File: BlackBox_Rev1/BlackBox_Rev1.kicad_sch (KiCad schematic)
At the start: 15 parts

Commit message: schematic design
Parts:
- removed C? (x2): 10uF, Capacitor_SMD:C_0603_1608Metric_Pad1.08x0.95mm_HandSolder, symbol Device:C
- removed SW?: SW_SP3T, MRDT_Connectors:MOLEX_uF_S_03_Vertical, symbol Switch:SW_SP3T
- removed U?: TSR1-2433, MRDT_Devices:TSR_1-2433, symbol Driveboard_2022-rescue:TSR1-2433-MRDT_Devices
- added C?: 1uF, Capacitor_SMD:C_0603_1608Metric_Pad1.08x0.95mm_HandSolder, symbol Device:C
- added C?: 22uF, Capacitor_THT:CP_Radial_D5.0mm_P2.00mm, symbol BMS_2022_Rev1-rescue:CP1-Device
- added C?: 10uF, Capacitor_SMD:C_0603_1608Metric_Pad1.08x0.95mm_HandSolder, symbol Device:C
- added D?: D, symbol Device:D
- added J?: Conn_02x08_Counter_Clockwise, symbol Connector_Generic:Conn_02x08_Counter_Clockwise
- added J?: Conn_02x05_Counter_Clockwise, symbol Connector_Generic:Conn_02x05_Counter_Clockwise
- added Q?: Q_PMOS_DGS, symbol Device:Q_PMOS_DGS
- added U?: TSR1-2433, MRDT_Devices:TSR_1-2433, symbol BMS_2022_Rev1-rescue:TSR1-2433-MRDT_Devices
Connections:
- net +12V: now also C?.1, U?.1 (Vin)
- net +3V3: now also C?.1, C?.1, D?.1 (K), D?.2 (A), J?.10 (Pin_10), J?.3 (Pin_3), Q?.1 (D), Q?.2 (G), Q?.3 (S), U?.3 (Vout)
- net GND: now also C?.2, C?.2, C?.2, J?.4 (Pin_4), J?.5 (Pin_5), U?.2 (GND)
- net Display_A: now reaches U?.0 (RX1)
- net Display_A: now also J?.14 (Pin_14)
- net Display_B: now reaches U?.1 (TX1)
- net Display_B: now also J?.16 (Pin_16)
- net Oscillator_input: now reaches U?.15 (A1)
- net Oscillator_input: now also J?.1 (Pin_1)
- net Oscilator_Output: now reaches U?.16 (A2)
- net Oscilator_Output: now also J?.2 (Pin_2)
- net Interupt: now reaches U?.17 (A3)
- net Interupt: now also J?.8 (Pin_8)
- net Send_Data: now reaches U?.18 (A4)
- net Send_Data: now also J?.6 (Pin_6)
- net Send_Clock: now reaches U?.19 (A5)
- net Send_Clock: now also J?.7 (Pin_7)
- net Display_C: now reaches U?.2 (OUT2)
- net Display_C: now also J?.13 (Pin_13)
- net Display_D1_Low: now reaches U?.24 (A10)
- net Display_D1_Low: now also J?.1 (Pin_1)
- net Display_D2_Low: now reaches U?.25 (A11)
- net Display_D2_Low: now also J?.2 (Pin_2)
- net Display_D3_Low: now reaches U?.26 (A12)
- net Display_D3_Low: now also J?.6 (Pin_6)
- net Display_D4_Low: now reaches U?.27 (A13)
- net Display_D4_Low: now also J?.8 (Pin_8)
- net Display_D: now reaches U?.3 (LRCLK2)
- net Display_D: now also J?.3 (Pin_3)
- net Display_E: now reaches U?.4 (BCLK2)
- net Display_E: now also J?.5 (Pin_5)
- net Display_F: now reaches U?.5 (IN2)
- net Display_F: now also J?.11 (Pin_11)
- net Display_G: now reaches U?.6 (OUT1D)
- net Display_G: now also J?.15 (Pin_15)
- net at Conn?.2: now also C?.1, U?.1 (Vin)
- new net Clock_SquareWave: J?.12 (Pin_12), J?.9 (Pin_9)
- no-connect marks 4 -> 7
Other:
- note added: "4 Digit LED display"
- note added: "DS1374 timer"
- note added: "Ethernet"
- note added: "Vcc SQW INT SCL SDA"
- note added: "X1 X2 Vbackup RST GND"
- note added: "power switch"
- note removed: "POWER"
- moved on the sheet: C?, Conn?, Conn?A, Conn?B, U?

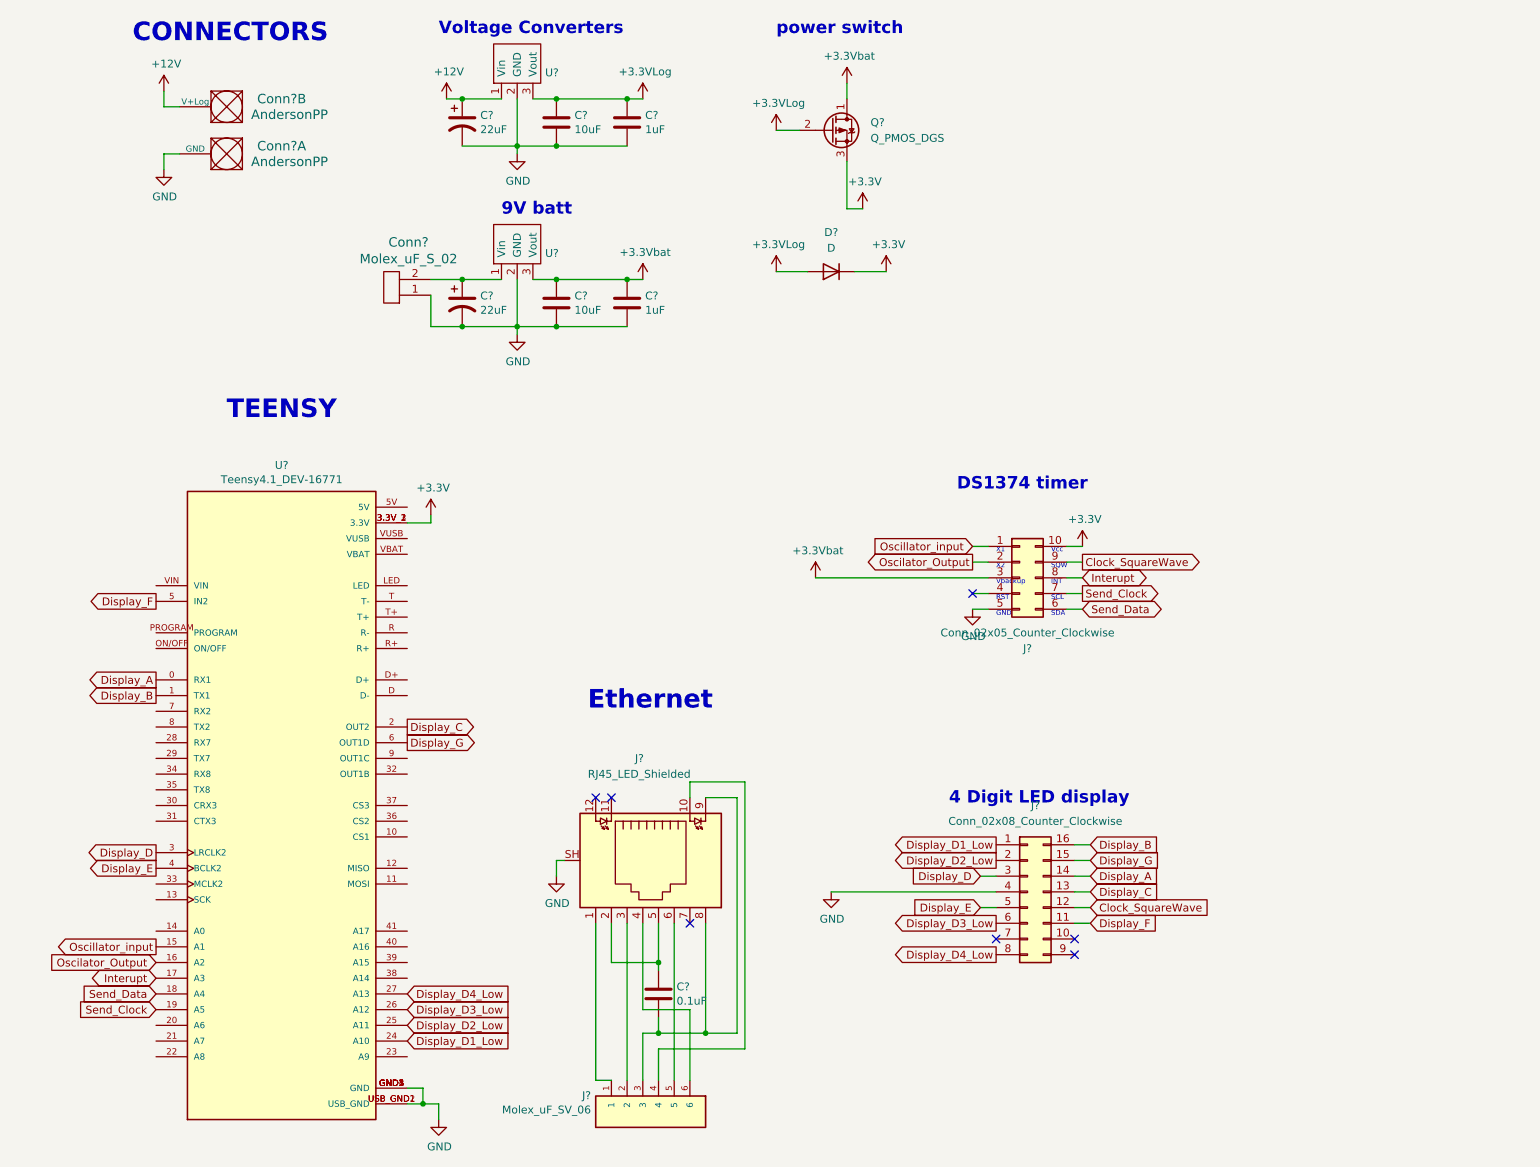
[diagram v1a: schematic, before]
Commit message: added LED and buttons
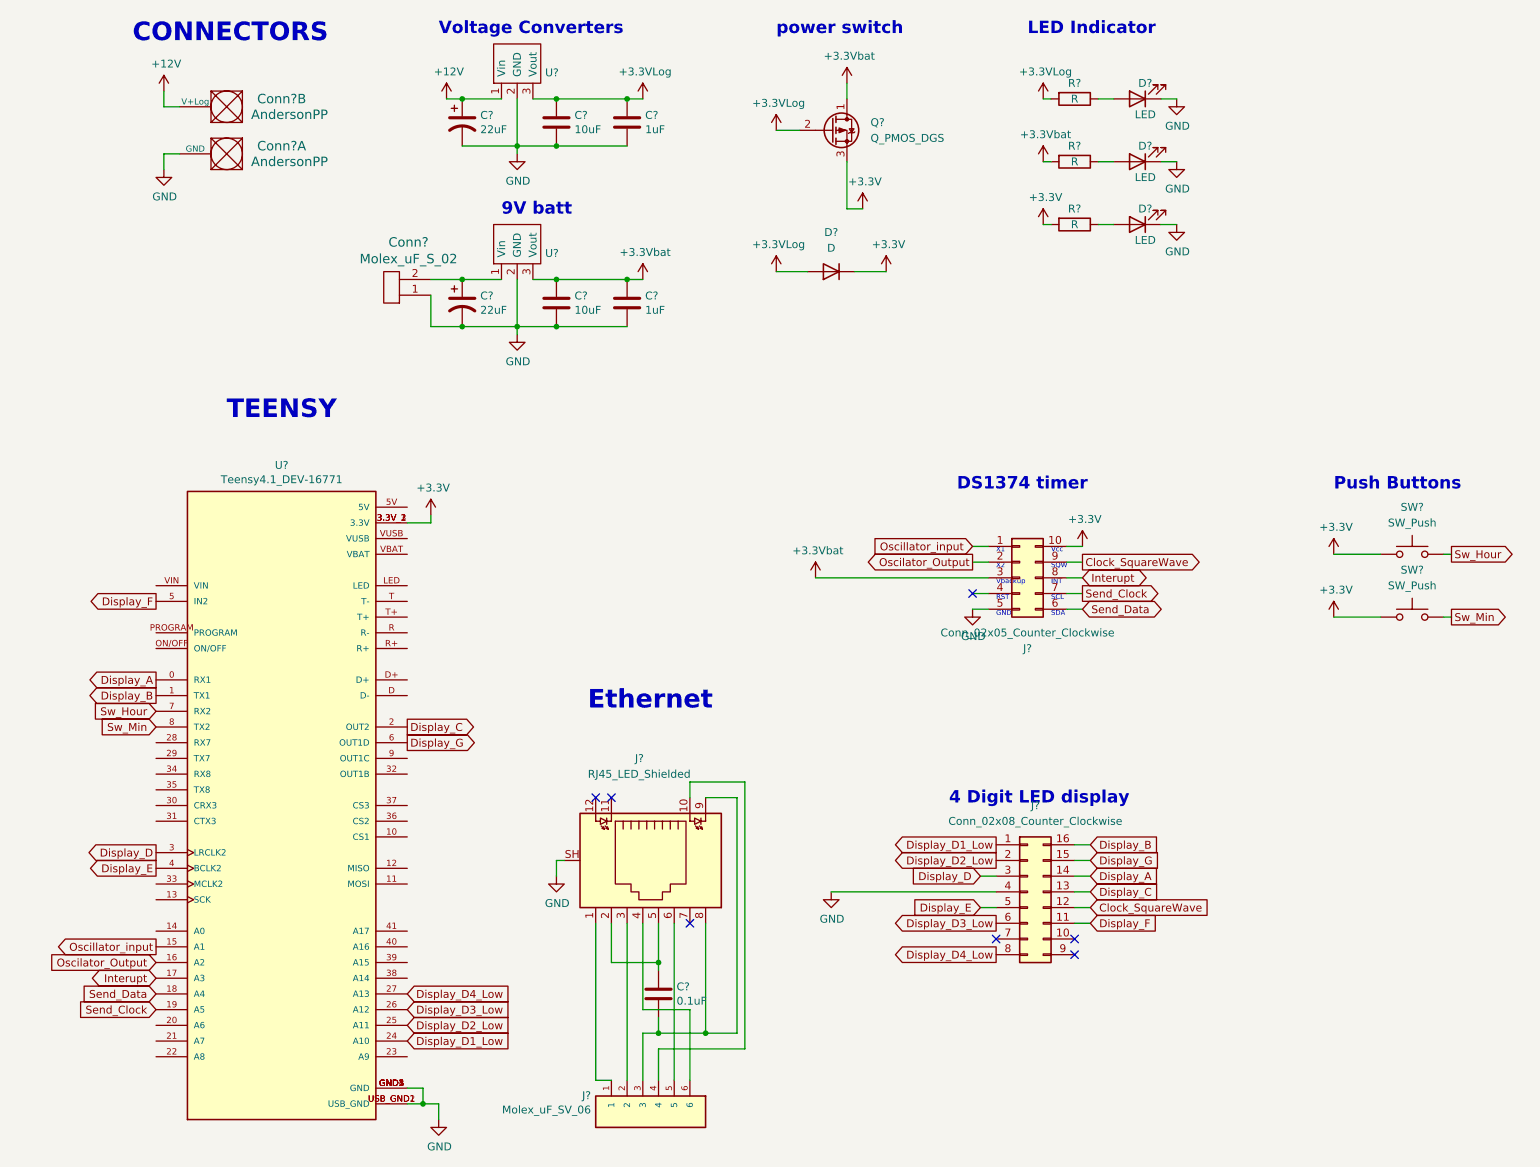
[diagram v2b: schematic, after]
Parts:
- added D? (x3): LED, symbol Device:LED
- added R? (x3): R, symbol Device:R
- added SW? (x2): SW_Push, symbol Switch:SW_Push
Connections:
- net +3V3: now also R?.2, R?.2, R?.2, SW?.1, SW?.1
- net GND: now also D?.1 (K), D?.1 (K), D?.1 (K)
- net Sw_Hour: now reaches U?.7 (RX2)
- net Sw_Hour: now also SW?.2
- net Sw_Min: now reaches U?.8 (TX2)
- net Sw_Min: now also SW?.2
- new net: D?.2 (A), R?.1 (x3)
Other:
- note added: "LED Indicator"
- note added: "Push Buttons"

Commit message: update bom
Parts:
- removed C?: 1uF, Capacitor_SMD:C_0603_1608Metric_Pad1.08x0.95mm_HandSolder, symbol Device:C
- removed C?: 22uF, Capacitor_THT:CP_Radial_D5.0mm_P2.00mm, symbol BMS_2022_Rev1-rescue:CP1-Device
- removed C?: 10uF, Capacitor_SMD:C_0603_1608Metric_Pad1.08x0.95mm_HandSolder, symbol Device:C
- removed J?: Conn_02x05_Counter_Clockwise, symbol Connector_Generic:Conn_02x05_Counter_Clockwise
- removed Q?: Q_PMOS_DGS, symbol Device:Q_PMOS_DGS
- removed U?: TSR1-2433, MRDT_Devices:TSR_1-2433, symbol BMS_2022_Rev1-rescue:TSR1-2433-MRDT_Devices
- added D2: D, Diode_SMD:D_SOD-123, symbol Device:D
- added Q1: Q_NMOS_GSD, symbol Device:Q_NMOS_GSD
- added R1: 1k, Resistor_SMD:R_0603_1608Metric_Pad0.98x0.95mm_HandSolder, symbol Device:R
- D1: renamed from D?; footprint (none) -> Diode_SMD:D_SOD-123
- D3, D4, D5: renamed from D?; footprint (none) -> LED_SMD:LED_0603_1608Metric_Pad1.05x0.95mm_HandSolder
- R2: renamed from R?; value R -> 3360; footprint (none) -> Resistor_SMD:R_0603_1608Metric_Pad0.98x0.95mm_HandSolder
- R3: renamed from R?; value R -> 1k; footprint (none) -> Resistor_SMD:R_0603_1608Metric_Pad0.98x0.95mm_HandSolder
- R4: renamed from R?; value R -> 330; footprint (none) -> Resistor_SMD:R_0603_1608Metric_Pad0.98x0.95mm_HandSolder
- SW1, SW2: renamed from SW?; footprint (none) -> Button_Switch_SMD:SW_SPST_TL3305A
- gave numbers to parts that had none: 11
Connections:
- net +3V3: no longer D1.1 (K), D1.2 (A), R2.2, R3.2, R4.2
- net VBat: now reaches Conn2.2
- net VBat: now also R3.2, Q1.3 (D)
- net Bat_Ctrl: now reaches U1.14 (A0)
- net Bat_Ctrl: now also Q1.1 (G)
- net +12V renamed Vin
- net Vin: now also D1.1 (K), R4.2, D2.1 (K), R1.1; no longer Conn1.2 (V+Log)
- net Interupt: no longer names the net of U1.17 (A3)
- net Oscilator_Output: no longer names the net of U1.16 (A2)
- net Oscillator_input: no longer names the net of U1.15 (A1)
- net Send_Clock: no longer names the net of U1.19 (A5)
- net Send_Data: no longer names the net of U1.18 (A4)
- new net: D2.2 (A), Q1.2 (S), R1.2
- new net VLog: Conn1.2 (V+Log), D1.2 (A), R2.2
- no-connect marks 7 -> 6
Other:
- note added: "9V battery"
- note removed: "9V batt"
- note removed: "DS1374 timer"
- note removed: "Vcc SQW INT SCL SDA"
- note removed: "X1 X2 Vbackup RST GND"
- moved on the sheet: C2, C3, C4, Conn1A, Conn1B, Conn2, D1, SW1, SW2, U2

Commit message: output pdf
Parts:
- removed Conn2: Molex_uF_S_02, MRDT_Connectors:MOLEX_uF_S_02_Vertical, symbol BMS_2022_Rev1-rescue:Molex_uF_S_02-MRDT_Connectors
- removed D1, D2: D, Diode_SMD:D_SOD-123, symbol Device:D
- removed Q1: Q_NMOS_GSD, symbol Device:Q_NMOS_GSD
- removed R1: 1k, Resistor_SMD:R_0603_1608Metric_Pad0.98x0.95mm_HandSolder, symbol Device:R
- added Conn2: 12mm_Coin_Cell_Battery_Holder, symbol MRDT_Connectors:12mm_Coin_Cell_Battery_Holder
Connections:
- net GND: now also Conn2.GND
- net VLog: no longer Conn1.2 (V+Log)
- net Vin: no longer C2.1, U2.1 (Vin)
- net at U1.VBAT: now also Conn2.+V
- new net +36V: C2.1, Conn1.2 (V+Log), U2.1 (Vin)
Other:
- note added: "Green"
- note added: "RTC Coincell"
- note removed: "9V battery"
- note removed: "power switch"
- moved on the sheet: C2, C3, C4, D3, D4, D5, R2, R3, R4, SW1, SW2, U2

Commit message: add footprint to layout
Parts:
- removed D4: LED, LED_SMD:LED_0603_1608Metric_Pad1.05x0.95mm_HandSolder, symbol Device:LED
- removed R3: 1k, Resistor_SMD:R_0603_1608Metric_Pad0.98x0.95mm_HandSolder, symbol Device:R
- Conn2: footprint (none) -> MRDT_Connectors:CR1220_Battery_Holder
- renumbered C2 to C1, C3 to C2, C4 to C3, C1 to C4, D3 to D1, D5 to D3, R2 to R1, R4 to R3
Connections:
- net VLog is gone; now on net +36V: R1.2
- net Vin is gone; now on net +3V3: R3.2
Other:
- moved on the sheet: D3, R3

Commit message: finish layout design
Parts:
- J3: footprint (none) -> blackbox_rev1:timerLED
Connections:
- net +3V3: no longer C2.1, C3.1, R3.2, U2.3 (Vout)
- net Clock_SquareWave: now also U1.7 (RX2)
- net Display_A: now also U1.5 (IN2); no longer U1.0 (RX1)
- net Display_B: now also U1.3 (LRCLK2); no longer U1.1 (TX1)
- net Display_C: now also U1.6 (OUT1D); no longer U1.2 (OUT2)
- net Display_D: now also U1.2 (OUT2); no longer U1.3 (LRCLK2)
- net Display_D1_Low: now also U1.0 (RX1); no longer U1.24 (A10)
- net Display_D2_Low: now also U1.1 (TX1); no longer U1.25 (A11)
- net Display_D3_Low: now also U1.10 (CS1); no longer U1.26 (A12)
- net Display_D4_Low: now also U1.11 (MOSI); no longer U1.27 (A13)
- net Display_E: now also U1.9 (OUT1C); no longer U1.4 (BCLK2)
- net Display_F: now also U1.8 (TX2); no longer U1.5 (IN2)
- net Display_G: now also U1.4 (BCLK2); no longer U1.6 (OUT1D)
- net Sw_Hour: now also U1.28 (RX7); no longer U1.7 (RX2)
- net Sw_Min: now also U1.29 (TX7); no longer U1.8 (TX2)
- net +5V: now reaches U1.VIN
- net +5V: now also C2.1, C3.1, R3.2, U2.3 (Vout)
